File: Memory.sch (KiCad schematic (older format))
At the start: 18 parts, among them U10 74LS05, U11 74HCT00, U12 74LS32, U2 AS6C4008-55PCN, U3 AS6C4008-55PCN, U4 AS6C4008-55PCN, U5 AS6C4008-55PCN, U6 74HCT00, U7 74LS32, U8 74LS32, U9 74LS05

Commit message: romen
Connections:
- net at U6.3, U7.1: now also U12.5; no longer U7.12
- net at U6.13, U6.6: now also U12.4; no longer U7.9
- net at U6.8: now also U7.12; no longer U7.13
- net at U12.6: now also U7.9
- new net ~ROMEN: U7.13
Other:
- moved on the sheet: U10D, U10E, U10F, U11D, U12B, U6C, U7C, U7D
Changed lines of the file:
@@
 L 74:74LS05 U10
 U 4 1 61113E16
-P 950 2850
-F 0 "U10" H 950 3167 50  0000 C CNN
-F 1 "74LS05" H 950 3076 50  0000 C CNN
-F 2 "" H 950 2850 50  0001 C CNN
-F 3 "http://www.ti.com/lit/gpn/sn74LS05" H 950 2850 50  0001 C CNN
-	4    950  2850
+P 900 2850
+F 0 "U10" H 900 3167 50  0000 C CNN
+F 1 "74LS05" H 900 3076 50  0000 C CNN
+F 2 "" H 900 2850 50  0001 C CNN
+F 3 "http://www.ti.com/lit/gpn/sn74LS05" H 900 2850 50  0001 C CNN
+	4    900  2850
 	1    0    0    -1
 $EndComp
@@
 L 74:74LS05 U10
 U 5 1 61115258
-P 950 3350
-F 0 "U10" H 950 3667 50  0000 C CNN
-F 1 "74LS05" H 950 3576 50  0000 C CNN
-F 2 "" H 950 3350 50  0001 C CNN
-F 3 "http://www.ti.com/lit/gpn/sn74LS05" H 950 3350 50  0001 C CNN
-	5    950  3350
+P 900 3350
+F 0 "U10" H 900 3667 50  0000 C CNN
+F 1 "74LS05" H 900 3576 50  0000 C CNN
+F 2 "" H 900 3350 50  0001 C CNN
+F 3 "http://www.ti.com/lit/gpn/sn74LS05" H 900 3350 50  0001 C CNN
+	5    900  3350
 	1    0    0    -1
 $EndComp
@@
 L 74:74LS05 U10
 U 6 1 61116A23
-P 950 3800
-F 0 "U10" H 950 4117 50  0000 C CNN
-F 1 "74LS05" H 950 4026 50  0000 C CNN
-F 2 "" H 950 3800 50  0001 C CNN
-F 3 "http://www.ti.com/lit/gpn/sn74LS05" H 950 3800 50  0001 C CNN
-	6    950  3800
+P 900 3850
+F 0 "U10" H 900 4167 50  0000 C CNN
+F 1 "74LS05" H 900 4076 50  0000 C CNN
+F 2 "" H 900 3850 50  0001 C CNN
+F 3 "http://www.ti.com/lit/gpn/sn74LS05" H 900 3850 50  0001 C CNN
+	6    900  3850
 	1    0    0    -1
 $EndComp
@@
 L 74:74HCT00 U11
 U 4 1 6142508F
-P 4750 4500
-F 0 "U11" H 4750 4825 50  0000 C CNN
-F 1 "74HCT00" H 4750 4734 50  0000 C CNN
-F 2 "" H 4750 4500 50  0001 C CNN
-F 3 "http://www.ti.com/lit/gpn/sn74hct00" H 4750 4500 50  0001 C CNN
-	4    4750 4500
+P 4200 5750
+F 0 "U11" H 4200 6075 50  0000 C CNN
+F 1 "74HCT00" H 4200 5984 50  0000 C CNN
+F 2 "" H 4200 5750 50  0001 C CNN
+F 3 "http://www.ti.com/lit/gpn/sn74hct00" H 4200 5750 50  0001 C CNN
+	4    4200 5750
 	1    0    0    -1
 $EndComp
@@
 L 74:74HCT00 U6
 U 3 1 61932778
-P 2600 4300
-F 0 "U6" H 2600 4625 50  0000 C CNN
-F 1 "74HCT00" H 2600 4534 50  0000 C CNN
-F 2 "" H 2600 4300 50  0001 C CNN
-F 3 "http://www.ti.com/lit/gpn/sn74hct00" H 2600 4300 50  0001 C CNN
-	3    2600 4300
+P 2000 4350
+F 0 "U6" H 2000 4125 50  0000 C CNN
+F 1 "74HCT00" H 2000 4034 50  0000 C CNN
+F 2 "" H 2000 4350 50  0001 C CNN
+F 3 "http://www.ti.com/lit/gpn/sn74hct00" H 2000 4350 50  0001 C CNN
+	3    2000 4350
 	1    0    0    -1
 $EndComp
@@
 	1700 3950 1400 3950
 Entry Wire Line
-	1300 4100 1400 4200
+	1300 4150 1400 4250
 Entry Wire Line
-	1300 4300 1400 4400
+	1300 4350 1400 4450
 Entry Wire Line
 	1300 3450 1400 3550
@@
 Wire Wire Line
 	2050 6400 2150 6400
-Text Label 1500 4200 0    50   ~ 0
+Text Label 1500 4250 0    50   ~ 0
 a21
-Text Label 1500 4400 0    50   ~ 0
+Text Label 1500 4450 0    50   ~ 0
 a20
 Text Label 1500 3550 0    50   ~ 0
@@
 ~CSRAM2
 Wire Wire Line
-	650  2850 650  3350
-Connection ~ 650  3350
-Wire Wire Line
-	650  3350 650  3800
-Connection ~ 650  3800
-Wire Wire Line
-	650  3800 650  4000
+	600  2850 600  3350
+Connection ~ 600  3350
 $Comp
 L OpenAmiga2000CoproAdapter-rescue:GND-power #PWR?
 U 1 1 61D81880
-P 650 4000
+P 600 4000
 AR Path="/61D81880" Ref="#PWR?"  Part="1"
 AR Path="/6068F728/61D81880" Ref="#PWR0114"  Part="1"
-F 0 "#PWR0114" H 650 3750 50  0001 C CNN
-F 1 "GND" H 655 3827 50  0000 C CNN
-F 2 "" H 650 4000 50  0001 C CNN
-F 3 "" H 650 4000 50  0001 C CNN
-	1    650  4000
+F 0 "#PWR0114" H 600 3750 50  0001 C CNN
+F 1 "GND" H 605 3827 50  0000 C CNN
+F 2 "" H 600 4000 50  0001 C CNN
+F 3 "" H 600 4000 50  0001 C CNN
+	1    600  4000
 	1    0    0    -1
 $EndComp
@@
 Wire Wire Line
 	2200 3950 2200 3550
-Text Notes 400  4750 0    50   ~ 0
+Text Notes 4450 3150 0    50   ~ 0
 ROM  | JP1 | JP2\n------------\n256K |   1  |  1\n512K |   2  |  1\n1M   |   2  |  2
 $Comp
@@
 L 74:74LS32 U12
 U 2 1 607A7AE3
-P 5750 5950
-F 0 "U12" H 5750 6275 50  0000 C CNN
-F 1 "74LS32" H 5750 6184 50  0000 C CNN
-F 2 "" H 5750 5950 50  0001 C CNN
-F 3 "http://www.ti.com/lit/gpn/sn74LS32" H 5750 5950 50  0001 C CNN
-	2    5750 5950
+P 3300 4150
+F 0 "U12" H 3300 4475 50  0000 C CNN
+F 1 "74LS32" H 3300 4384 50  0000 C CNN
+F 2 "" H 3300 4150 50  0001 C CNN
+F 3 "http://www.ti.com/lit/gpn/sn74LS32" H 3300 4150 50  0001 C CNN
+	2    3300 4150
 	1    0    0    -1
 $EndComp
@@
 L 74:74LS32 U7
 U 4 1 6050398D
-P 3300 4200
-F 0 "U7" H 3300 4525 50  0000 C CNN
-F 1 "74LS32" H 3300 4434 50  0000 C CNN
-F 2 "" H 3300 4200 50  0001 C CNN
-F 3 "http://www.ti.com/lit/gpn/sn74LS32" H 3300 4200 50  0001 C CNN
-	4    3300 4200
+P 2600 4450
+F 0 "U7" H 2600 4775 50  0000 C CNN
+F 1 "74LS32" H 2600 4684 50  0000 C CNN
+F 2 "" H 2600 4450 50  0001 C CNN
+F 3 "http://www.ti.com/lit/gpn/sn74LS32" H 2600 4450 50  0001 C CNN
+	4    2600 4450
 	1    0    0    -1
 $EndComp
@@
 	2900 3800 3000 3800
 Wire Wire Line
-	4200 3800 4200 4100
-Wire Wire Line
-	3000 3800 3000 4000
-Wire Wire Line
-	3000 4000 3600 4000
-Connection ~ 3000 3800
-Wire Wire Line
 	4200 3200 5500 3200
 Wire Wire Line
@@
 	1400 3200 2900 3200
 Wire Wire Line
-	2900 4300 3000 4300
-Wire Wire Line
-	1400 4400 2300 4400
-Wire Wire Line
-	1400 4200 2300 4200
-Wire Wire Line
-	3000 4100 2900 4100
+	1400 4450 1700 4450
+Wire Wire Line
+	1400 4250 1700 4250
 $Comp
 L 74:74LS32 U7
 U 3 1 604F5E6E
-P 3900 4100
-F 0 "U7" H 3900 3783 50  0000 C CNN
-F 1 "74LS32" H 3900 3874 50  0000 C CNN
-F 2 "" H 3900 4100 50  0001 C CNN
-F 3 "http://www.ti.com/lit/gpn/sn74LS32" H 3900 4100 50  0001 C CNN
-	3    3900 4100
+P 3900 4250
+F 0 "U7" H 3900 3933 50  0000 C CNN
+F 1 "74LS32" H 3900 4024 50  0000 C CNN
+F 2 "" H 3900 4250 50  0001 C CNN
+F 3 "http://www.ti.com/lit/gpn/sn74LS32" H 3900 4250 50  0001 C CNN
+	3    3900 4250
 	1    0    0    -1
 $EndComp
@@
 	1    0    0    -1
 $EndComp
+Connection ~ 3000 3800
+Wire Wire Line
+	4200 3800 4200 4250
+Wire Wire Line
+	3000 3800 3000 4050
+Wire Wire Line
+	2900 4250 3000 4250
+Wire Wire Line
+	2900 3000 2900 4250
+Wire Wire Line
+	2900 4450 3600 4450
+Wire Wire Line
+	3600 4350 3600 4450
+Connection ~ 600  3850
+Wire Wire Line
+	600  3850 600  4000
+Wire Wire Line
+	600  3350 600  3850
+Wire Wire Line
+	2300 4550 2300 4900
+Wire Wire Line
+	2300 4900 1850 4900
+Text Label 1850 4900 0    50   ~ 0
+~ROMEN
 Wire Bus Line
-	1300 2700 1300 4750
+	1300 2700 1300 4350
 Wire Bus Line
 	10700 1050 10700 6350
@@
 Wire Bus Line
 	8900 600  8900 5950
-Wire Wire Line
-	2900 3000 2900 4100
 $EndSCHEMATC

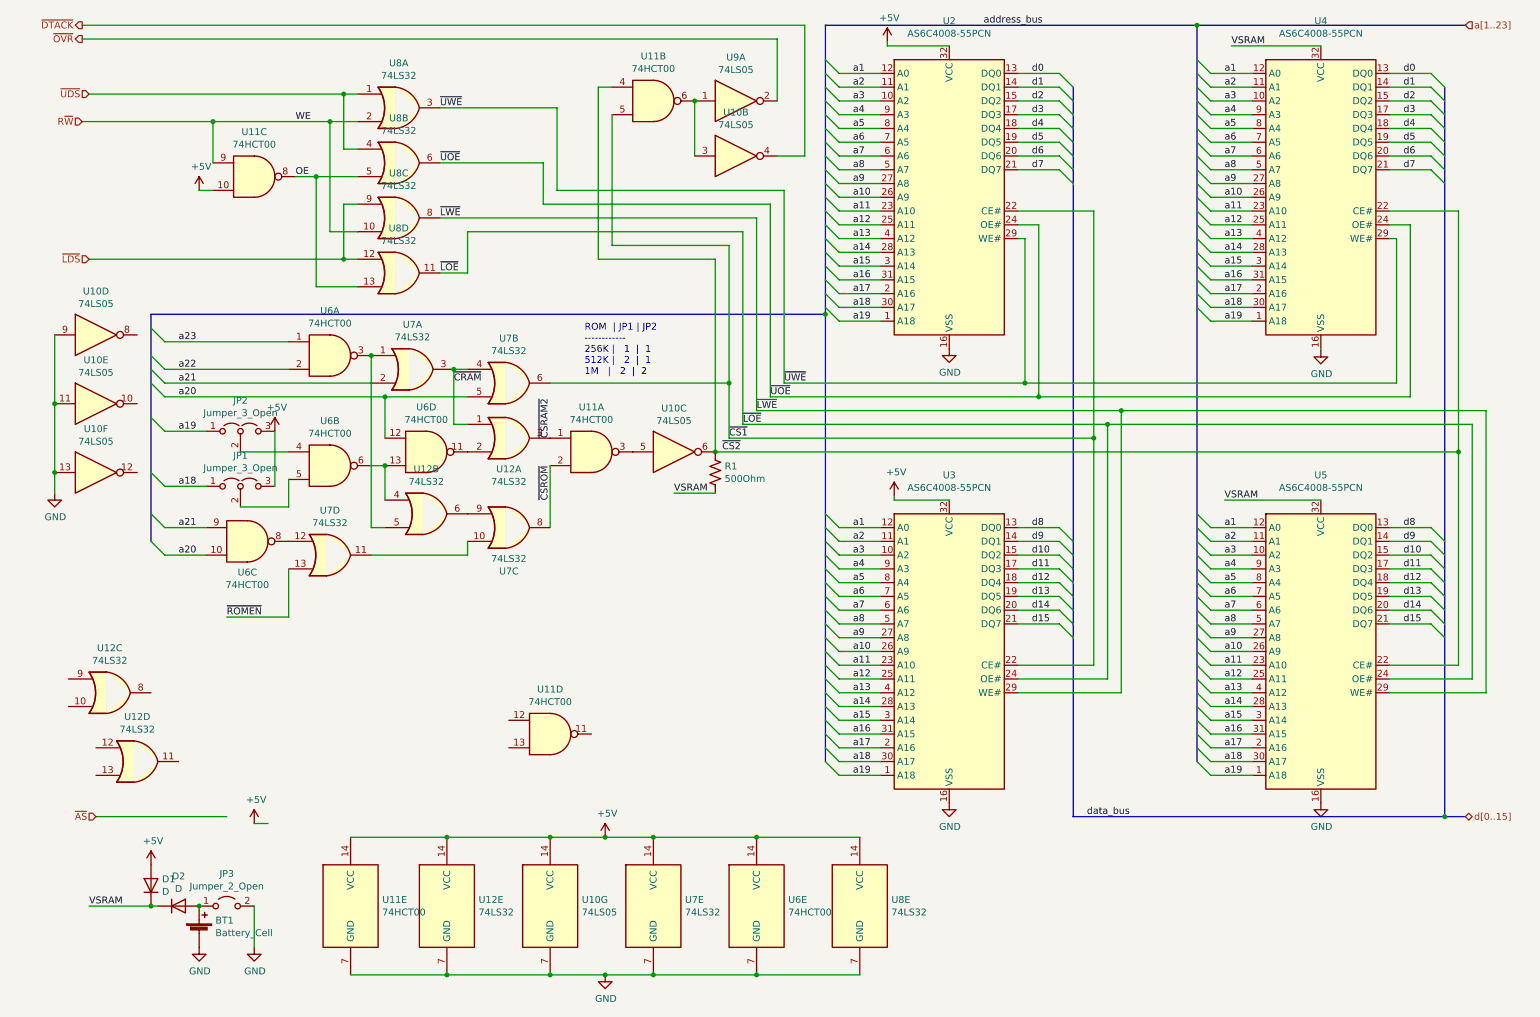
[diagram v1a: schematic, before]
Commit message: ROM RW switch
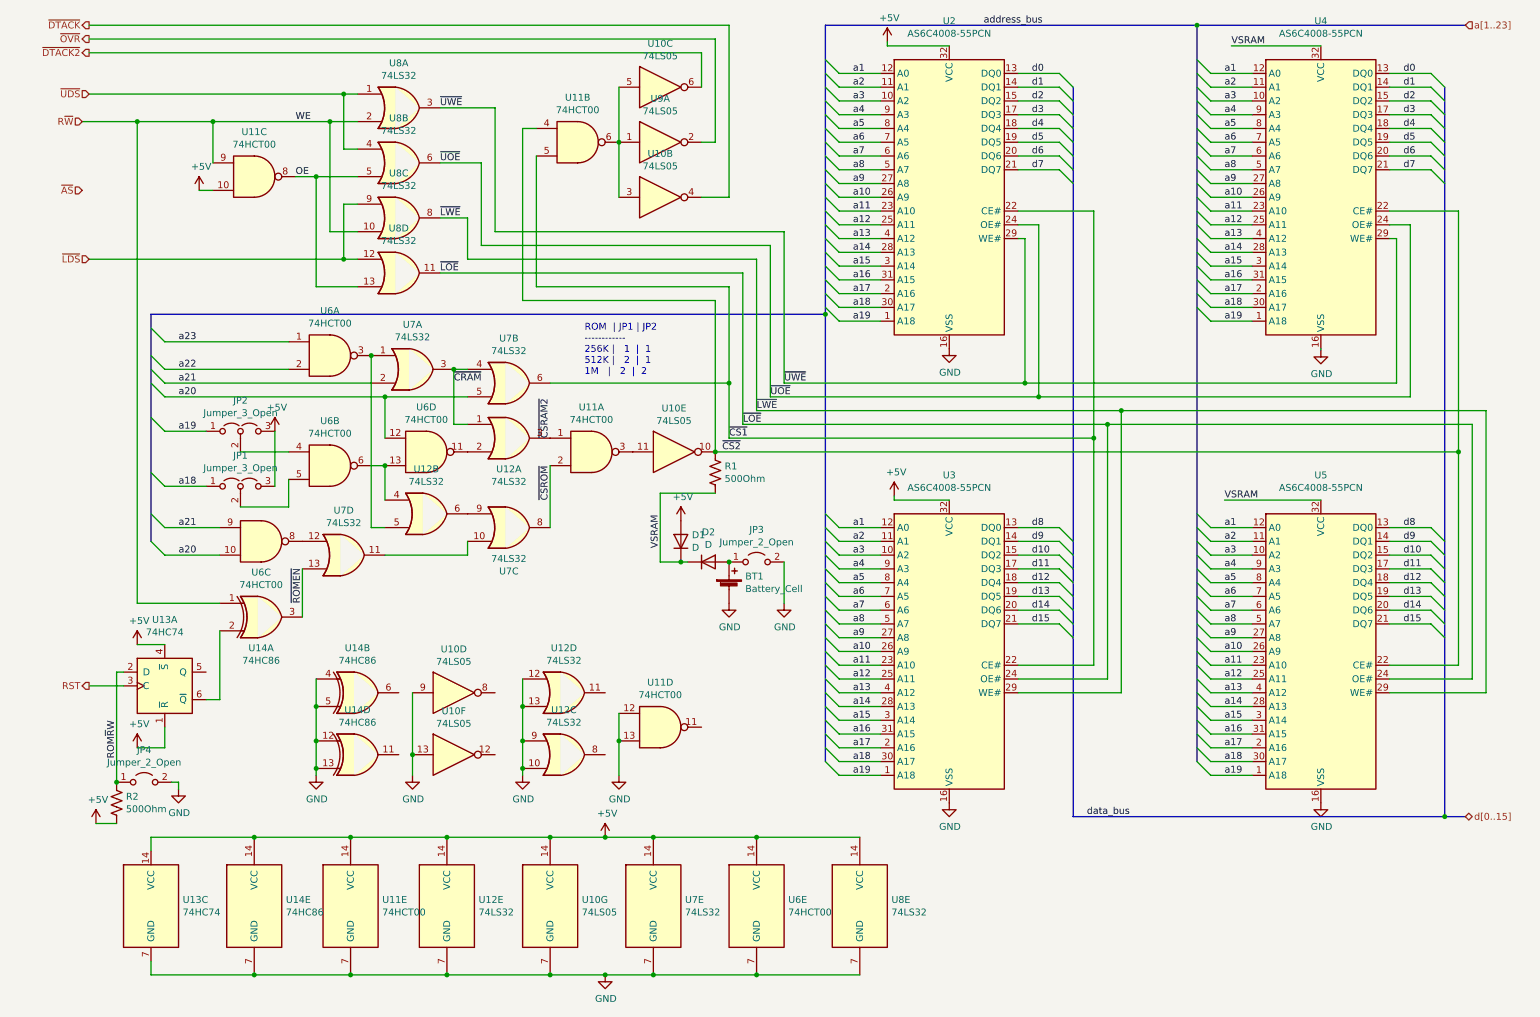
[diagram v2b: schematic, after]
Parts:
- added JP4: Jumper_2_Open, symbol jumper:Jumper_2_Open
- added R2: 500Ohm, symbol device:R_US
- added U13: 74HC74, symbol 74:74HC74
- added U14: 74HC86, symbol 74:74HC86
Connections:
- net +5V: now also R2.2, U13.1 (~R), U13.14 (VCC), U13.4 (~S), U14.14 (VCC)
- net GND: now also U11.12, U11.13, U12.10, U12.12, U12.13, U12.9, JP4.2 (B), U13.7 (GND), U14.12, U14.13, U14.4, U14.5, U14.7 (GND); no longer U10.11
- net R~W: now also U14.1
- net ~CS2: now also U10.10; no longer U10.6
- net ~ROMEN: now also U14.3
- net at U10.3, U11.6, U9.1: now also U10.5
- net at U11.3: now also U10.11; no longer U10.5
- new net: U13.6 (~Q), U14.2
- new net ROM~R~W: JP4.1 (A), R2.1, U13.2 (D)
- new net RST: U13.3 (C)
- new net ~DTACK2: U10.6
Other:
- moved on the sheet: BT1, D1, D2, JP3, U10B, U10C, U10D, U10E, U10F, U11B, U11D, U12C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

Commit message: replace 2 ORs by 3 way OR to share the IC
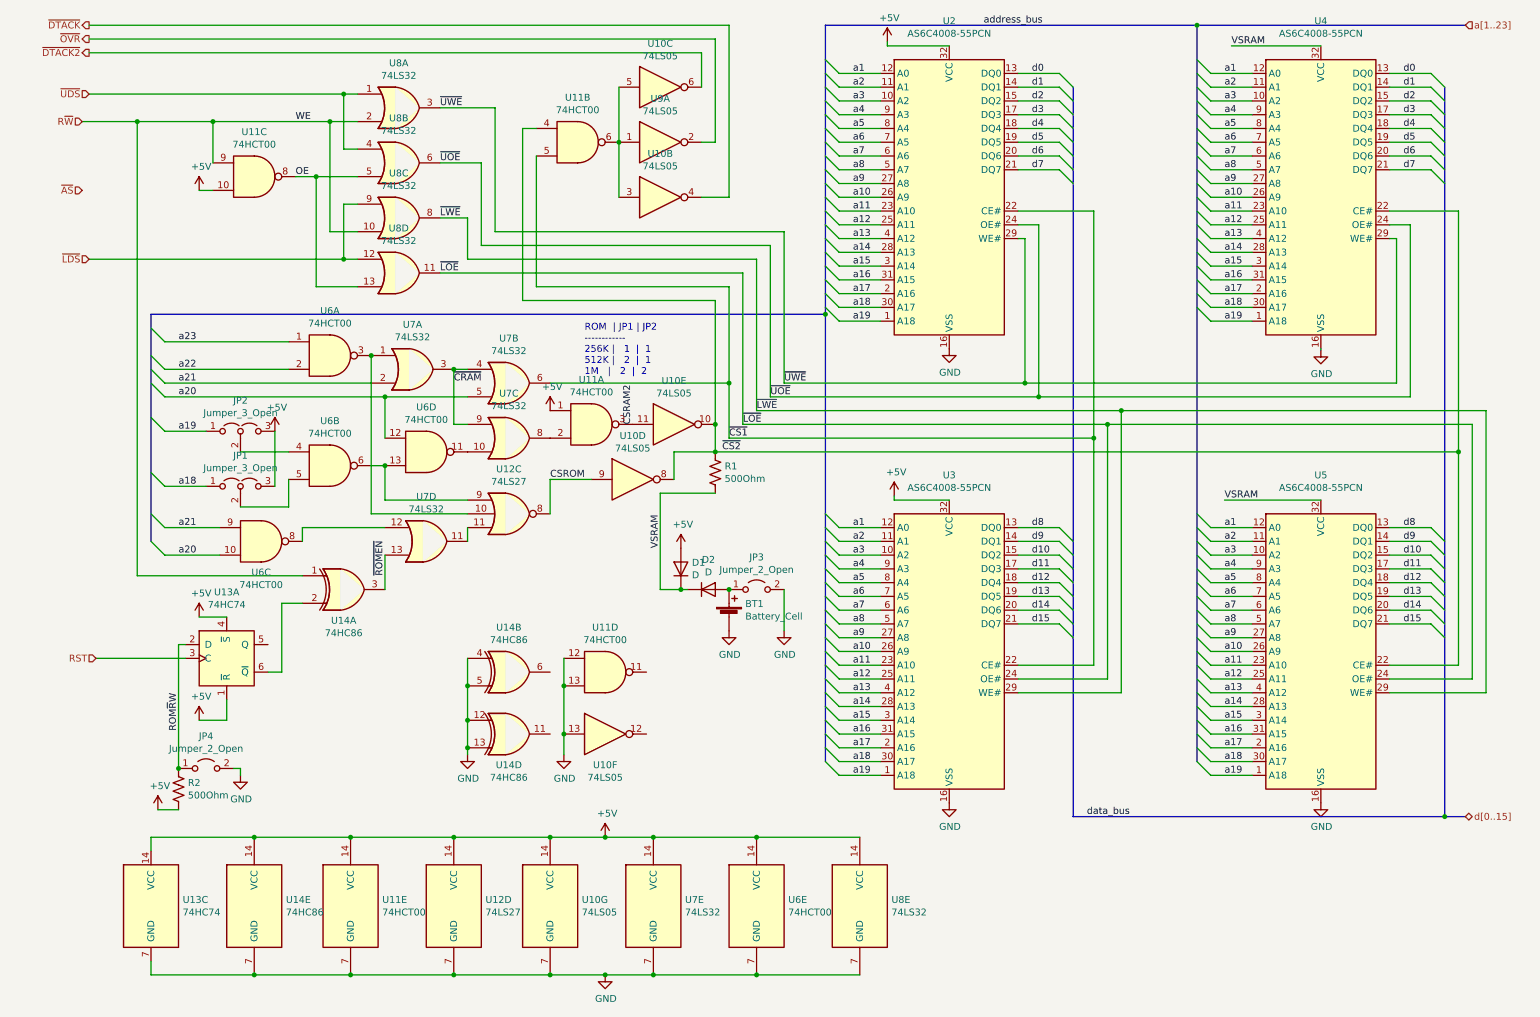
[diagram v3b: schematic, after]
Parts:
- removed U12: 74LS32, symbol 74:74LS32
- added U12: 74LS27, symbol 74:74LS27
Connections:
- net ~CSRAM2 is gone; now on net +5V: U11.1
- net +5V: now also U12.14 (VCC)
- net GND: now also U12.7 (GND); no longer U10.9
- net ~CRAM: now also U7.9
- net ~CS2: now also U10.8
- net at U6.3, U7.1: now also U12.10
- net at U7.11: now also U12.11; no longer U7.10
- net at U6.13, U6.6: now also U12.9
- net CSRAM2: now reaches U10.11, U11.3
- net at U6.11: now also U7.10
- net ~CSROM: no longer names the net of U11.2, U7.8
- new net CSROM: U10.9, U12.8
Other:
- moved on the sheet: BT1, D1, D2, JP3, JP4, R2, U10D, U10E, U10F, U11A, U11D, U13A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

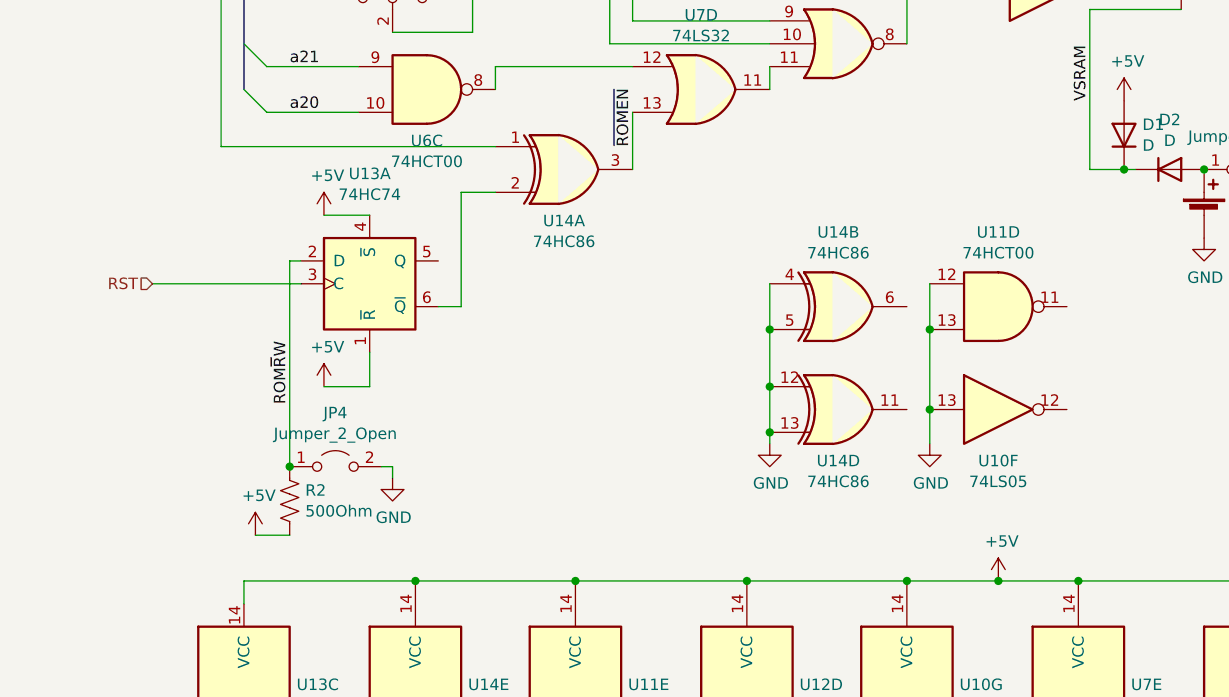
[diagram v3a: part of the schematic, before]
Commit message: RST low active
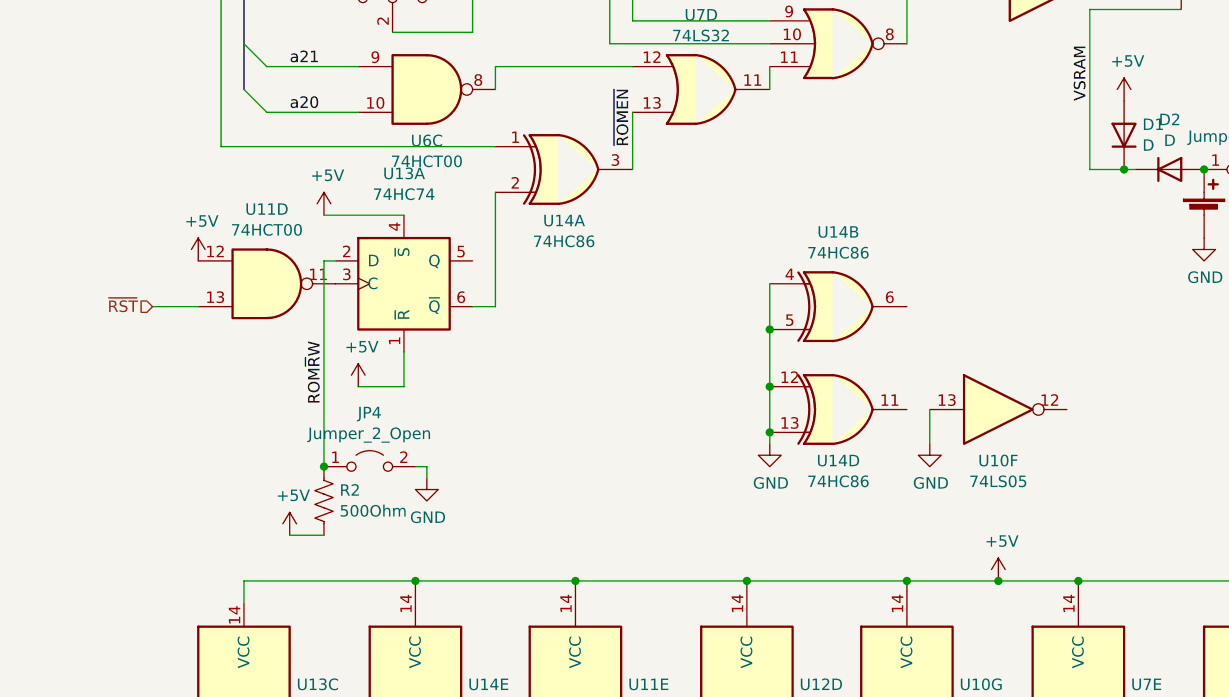
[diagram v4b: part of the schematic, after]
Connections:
- net RST is gone; now on an unnamed net: U13.3 (C)
- net +5V: now also U11.12
- net GND: no longer U11.12, U11.13
- new net ~RST: U11.13
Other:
- moved on the sheet: JP4, R2, U11D, U13A
